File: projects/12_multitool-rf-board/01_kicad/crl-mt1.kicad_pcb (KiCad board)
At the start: 4 copper layers, 68 parts, among them M1 vibro, SW1 RFswitch, SW2 RFswitch, U1 STM32WB55RG, U10 ESD, U5 ST7565R, U9 loadsw, X10 BAT+NTC, X6 FFC 18p, Y1 32MHz, Y2 32.768kHz

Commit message: proj12: transcribe all 8 chip pinouts from datasheets - board complete, 0 pending
Datasheet pads transcribed into pinmap.AUTHORED (with support parts in design.py):
- CC1101 QFN-20 (SWRS061I T19): AVDD x4, GND+EP, +DCOUPL cap
- ST25R3916 UFQFPN-32 (DS12484 Fig4): VDD x8, VSS x6+EP, I2C_EN=GND, AGDC cap,
  SCLK/MISO/MOSI/BSS(SS)/IRQ/RFO1/RFO2/RFI1/RFI2/XTI/XTO mapped exactly
- BQ25896 WQFN-24 (SLUSC76C): +buck inductor, bootstrap, REGN cap, ILIM R, TS divider, CE
- BQ27220 DSBGA-9 (SLUSCB7A): +VDD cap, GPOUT pull-up, BIN pull-down
- LM3281 DSBGA-6 (SNVSA38, was wrongly DSBGA-5): +MODE pin
- LP5562 DSBGA-12 (SNVS820B): +ADDR_SEL0/1, custom 3x4 ball footprint (A1-C4)
- RS3221-3.3 SOT-23-3 (RevA.3, was wrongly DFN-6)

pinmap: multi-pad net support; make_footprints: BGA grid generator.
88 parts, 118 nets, ERC 0 errors; PCB places 87 parts; all pads cross-check clean.

Co-Authored-By: Claude Opus 4.8 <noreply@anthropic.com>
Claude-Session: https://claude.ai/code/session_01Hk6s8R6up8HYVQWXd3atVk
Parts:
- added C_AGDC: 1uF, Capacitor_SMD:C_0402_1005Metric, F.Cu at (47.4, 103.1)
- added C_BTST: 47nF, Capacitor_SMD:C_0402_1005Metric, F.Cu at (70.3, 150.3)
- added C_CCd: 100nF, Capacitor_SMD:C_0402_1005Metric, F.Cu at (44.3, 53.1)
- added C_FGV: 2.2uF, Capacitor_SMD:C_0402_1005Metric, F.Cu at (154.0, 150.3)
- added C_REGN: 4.7uF, Capacitor_SMD:C_0805_2012Metric, F.Cu at (80.5, 150.8)
- added DA7: LP5562, crl-mt1:LP5562_DSBGA12, F.Cu at (163.3, 68.9)
- added DA8: RS3221-3.3, Package_TO_SOT_SMD:SOT-23, F.Cu at (224.6, 151.5)
- added L_CHG: 2.2uH, Inductor_SMD:L_0805_2012Metric, F.Cu at (60.6, 150.7)
- added R_FGB: 10k, Resistor_SMD:R_0402_1005Metric, F.Cu at (172.7, 150.3)
- added R_FGO: 10k, Resistor_SMD:R_0402_1005Metric, F.Cu at (163.3, 150.3)
- added R_ILIM: 1.1k, Resistor_SMD:R_0402_1005Metric, F.Cu at (90.4, 150.3)
- added R_TS1: 5.23k, Resistor_SMD:R_0402_1005Metric, F.Cu at (99.7, 150.3)
- added R_TS2: 30.31k, Resistor_SMD:R_0402_1005Metric, F.Cu at (109.2, 150.3)
- added U2: CC1101, Package_DFN_QFN:QFN-20-1EP_4x4mm_P0.5mm_EP2.5x2.5mm, F.Cu at (34.3, 55.2)
- added U3: ST25R3916, Package_DFN_QFN:QFN-32-1EP_5x5mm_P0.5mm_EP3.1x3.1mm, F.Cu at (35.6, 105.8)
- added U6: BQ25896, Package_DFN_QFN:QFN-24-1EP_4x4mm_P0.5mm_EP2.65x2.65mm, F.Cu at (50.1, 152.5)
- added U7: BQ27220, Package_BGA:BGA-9_1.6x1.6mm_Layout3x3_P0.5mm, F.Cu at (143.6, 151.2)
- added U8: LM3281, Package_BGA:Texas_DSBGA-6_0.76x1.16mm_Layout2x3_P0.4mm, F.Cu at (182.7, 150.7)
- added U8B: LM3281, Package_BGA:Texas_DSBGA-6_0.76x1.16mm_Layout2x3_P0.4mm, F.Cu at (202.8, 150.7)
- moved U9 144.6 mm to (245.7, 151.5)
- moved R37 144.6 mm to (236.3, 151.0)
- moved R_CC2 144.6 mm to (273.5, 150.3)
- moved U10 144.6 mm to (255.0, 151.5)
- moved R_CC1 144.6 mm to (264.0, 150.3)
- moved L14 130.4 mm to (212.8, 150.7)
- moved L13 119.9 mm to (192.7, 150.7)
- moved BT1 69.9 mm to (132.4, 152.0)
- moved X10 69.9 mm to (120.5, 153.0)
- moved ANT_NFC 23.5 mm to (83.2, 104.7)
- moved X_NFC1 23.5 mm to (70.5, 104.1)
- moved ZQ1 23.5 mm to (58.6, 104.2)
- moved FLT2 20.0 mm to (53.0, 53.5)
- moved SW2 20.0 mm to (71.9, 53.9)
- moved J_SUBG 20.0 mm to (99.3, 55.1)
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
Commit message: proj12: board outline + KRT placement inputs (groups/intent)
- make_pcb.py: add 110x46mm rounded board outline (Edge.Cuts)
- make_place_inputs.py: emit crl-mt1.groups.json from functional groups
  (8 groups, 87 parts) for the KiCadRoutingTools placer; check_groups: 0 errors
- crl-mt1.groups.json + crl-mt1.intent.json (floor-plan intent)

First placement pass produced candidates but needs more anneal moves to fully
de-overlap 87 parts; higher-move run in progress.

Co-Authored-By: Claude Opus 4.8 <noreply@anthropic.com>
Claude-Session: https://claude.ai/code/session_01Hk6s8R6up8HYVQWXd3atVk
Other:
- board outline added: 110 x 46 mm

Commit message: proj12: lock connectors/antennas/buttons on board edges for placement
make_pcb.py: 15 edge parts (USB-C, FFC, GPIO header, SWD, battery, U.FL,
3 antennas, 6 buttons) placed on the outline perimeter and KiCad-locked;
unlocked parts piled below the board as the placer's from-scratch start.
This gives the KiCadRoutingTools placer real edge anchors to organize the
functional groups around (the first unanchored run couldn't converge).

Co-Authored-By: Claude Opus 4.8 <noreply@anthropic.com>
Claude-Session: https://claude.ai/code/session_01Hk6s8R6up8HYVQWXd3atVk
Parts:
- moved X10 133.6 mm to (32.0, 53.0), turned to 90 degrees
- moved SW_U 129.0 mm to (110.0, 32.0)
- moved SW_D 127.0 mm to (116.0, 32.0)
- moved SW_L 125.1 mm to (122.0, 32.0)
- moved SW_R 123.3 mm to (128.0, 32.0)
- moved SW_O 109.1 mm to (104.0, 32.0)
- moved SW_B 105.5 mm to (98.0, 32.0)
- moved ANT_LF 99.3 mm to (101.0, 32.0)
- moved J_USB 94.7 mm to (85.0, 74.0)
- moved ANT_NFC 73.1 mm to (91.0, 32.0)
- moved LS1 66.6 mm to (54.1, 172.5)
- moved Q_SPK 66.6 mm to (65.1, 171.7)
- moved Q_VIB 66.6 mm to (43.4, 171.7)
- moved M1 66.6 mm to (34.0, 172.0)
- moved J_GPIO 63.8 mm to (137.5, 53.0), turned to 90 degrees
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
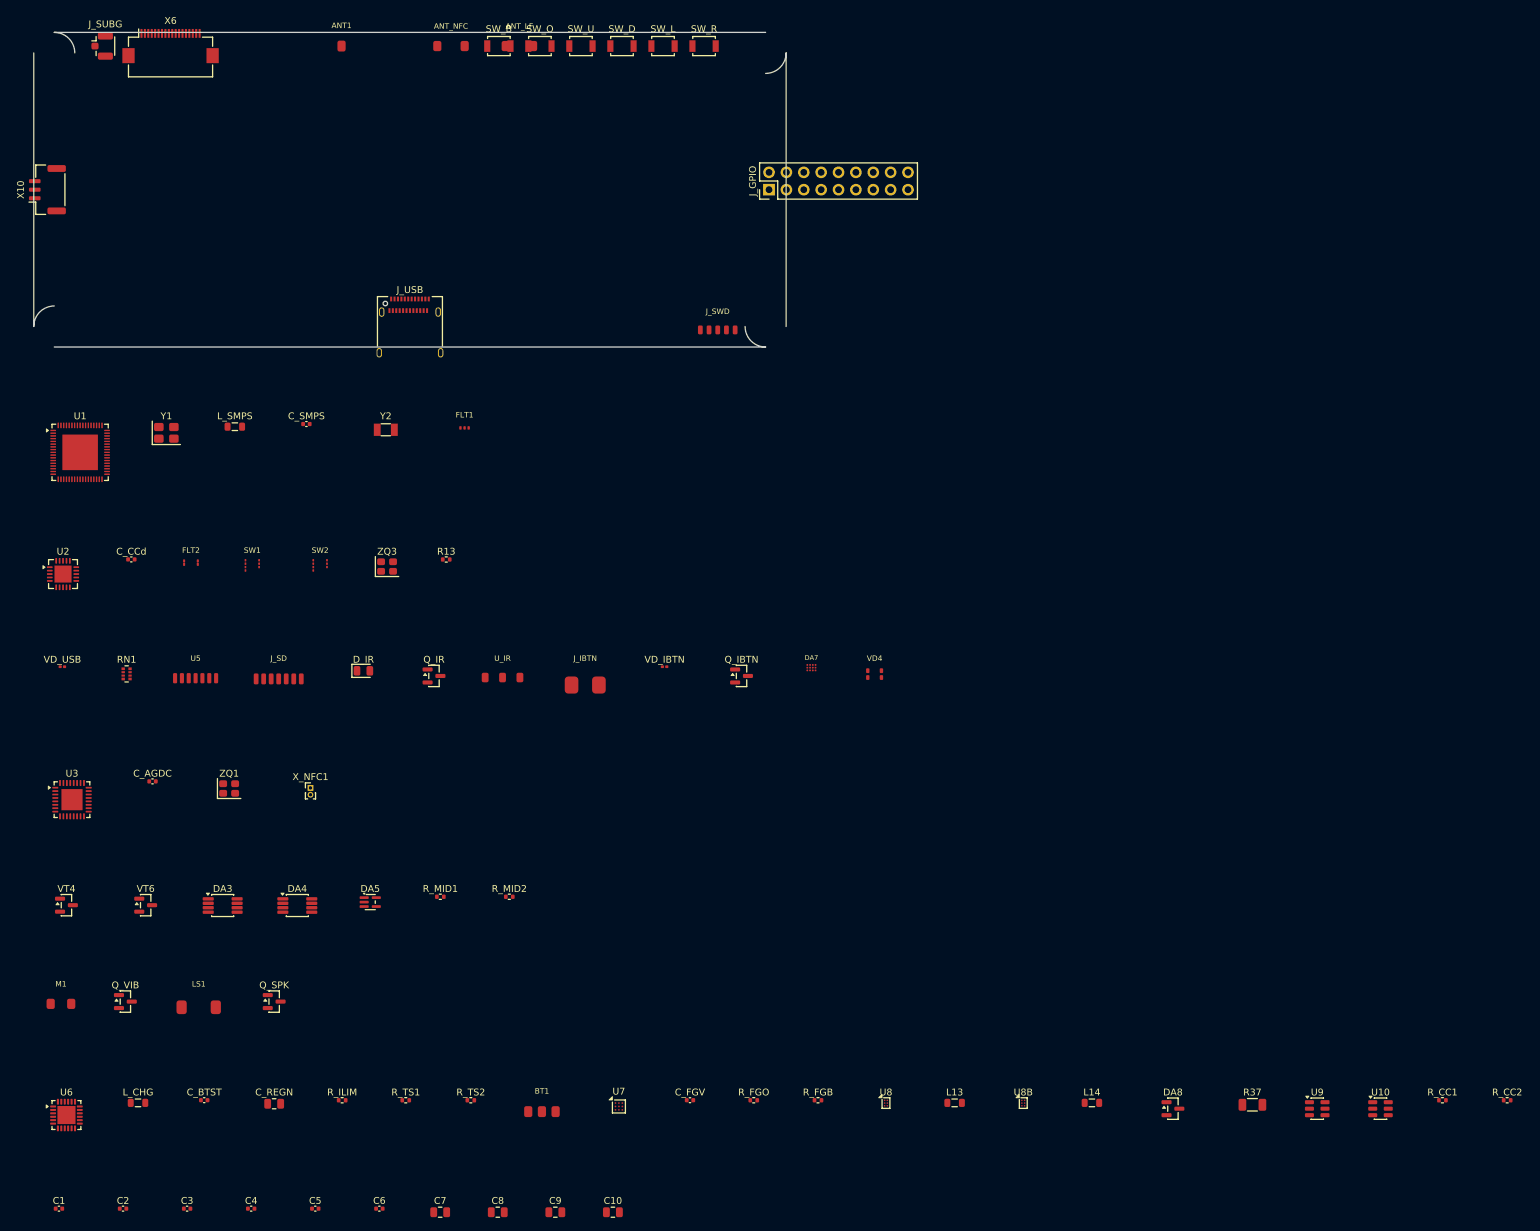
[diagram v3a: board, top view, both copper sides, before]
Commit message: proj12: deterministic legal placement - buildable, 0 overlaps
make_pcb.py: replace stochastic-placer dependence with a deterministic,
legal-by-construction placement - unlocked parts flow in grouped rows inside
an inset interior with courtyard+GAP spacing (no overlaps), connectors locked
on the edges. Closed rectangular outline (arcs left the polygon open ->
containment failed). 150x150mm board sized to hold all 87 parts + routing room.
check_assembly VERDICT: buildable (blocking 0, courtyard 0, 0 off-outline).

The KRT stochastic placer couldn't converge an 87-part board (group-cohesion
weight piled cluster members); the deterministic pack is reliable and feeds
the autorouter directly.

Co-Authored-By: Claude Opus 4.8 <noreply@anthropic.com>
Claude-Session: https://claude.ai/code/session_01Hk6s8R6up8HYVQWXd3atVk
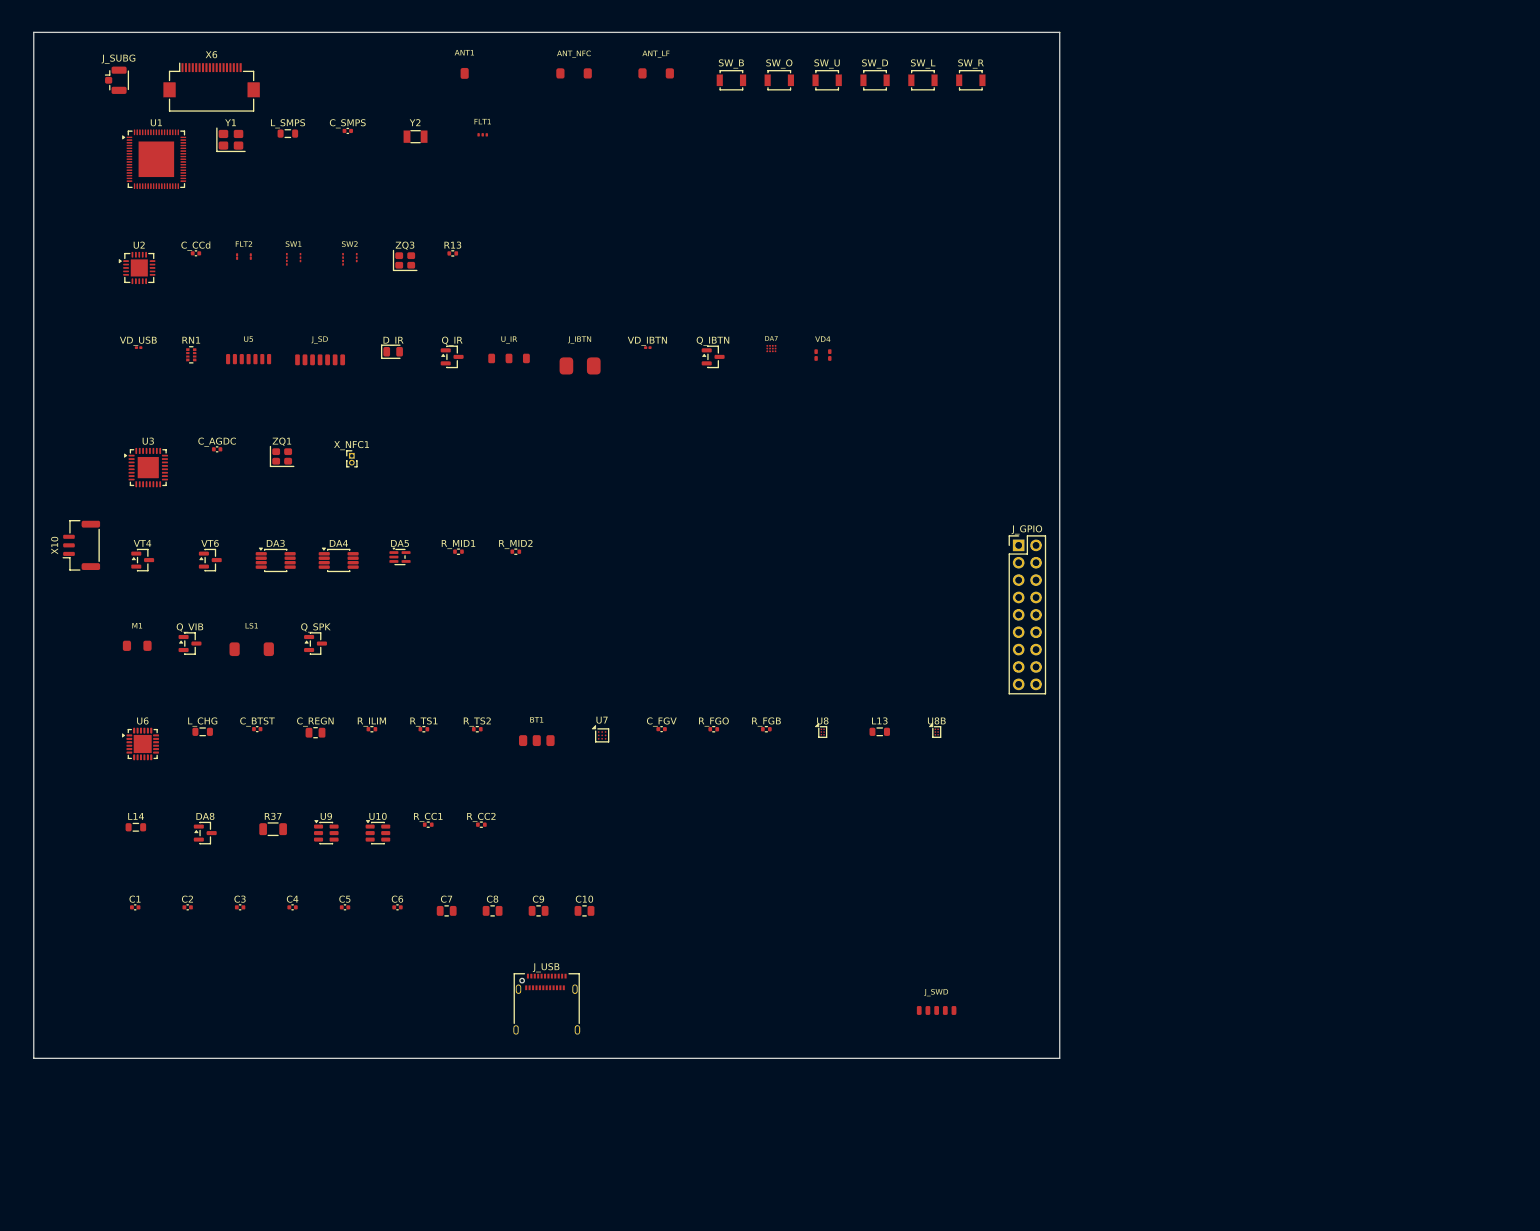
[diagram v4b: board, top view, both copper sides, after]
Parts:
- moved R_CC2 155.3 mm to (95.4, 145.8)
- moved R_CC1 153.7 mm to (87.7, 145.8)
- moved U10 152.0 mm to (80.3, 147.1)
- moved U9 150.4 mm to (72.8, 147.1)
- moved R37 148.7 mm to (65.0, 146.5)
- moved DA8 147.1 mm to (55.1, 147.1)
- moved L14 145.5 mm to (44.9, 146.2)
- moved J_SWD 104.5 mm to (162.0, 173.0)
- moved J_USB 101.0 mm to (105.0, 173.0)
- moved J_GPIO 63.5 mm to (174.0, 105.0), turned to 0 degrees
- moved U8B 55.7 mm to (162.0, 132.3)
- moved U6 55.4 mm to (45.9, 134.0)
- moved L13 55.3 mm to (153.7, 132.3)
- moved L_CHG 55.1 mm to (54.7, 132.3)
- moved U8 55.0 mm to (145.3, 132.3)
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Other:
- board size 110 x 46 mm -> 150 x 150 mm

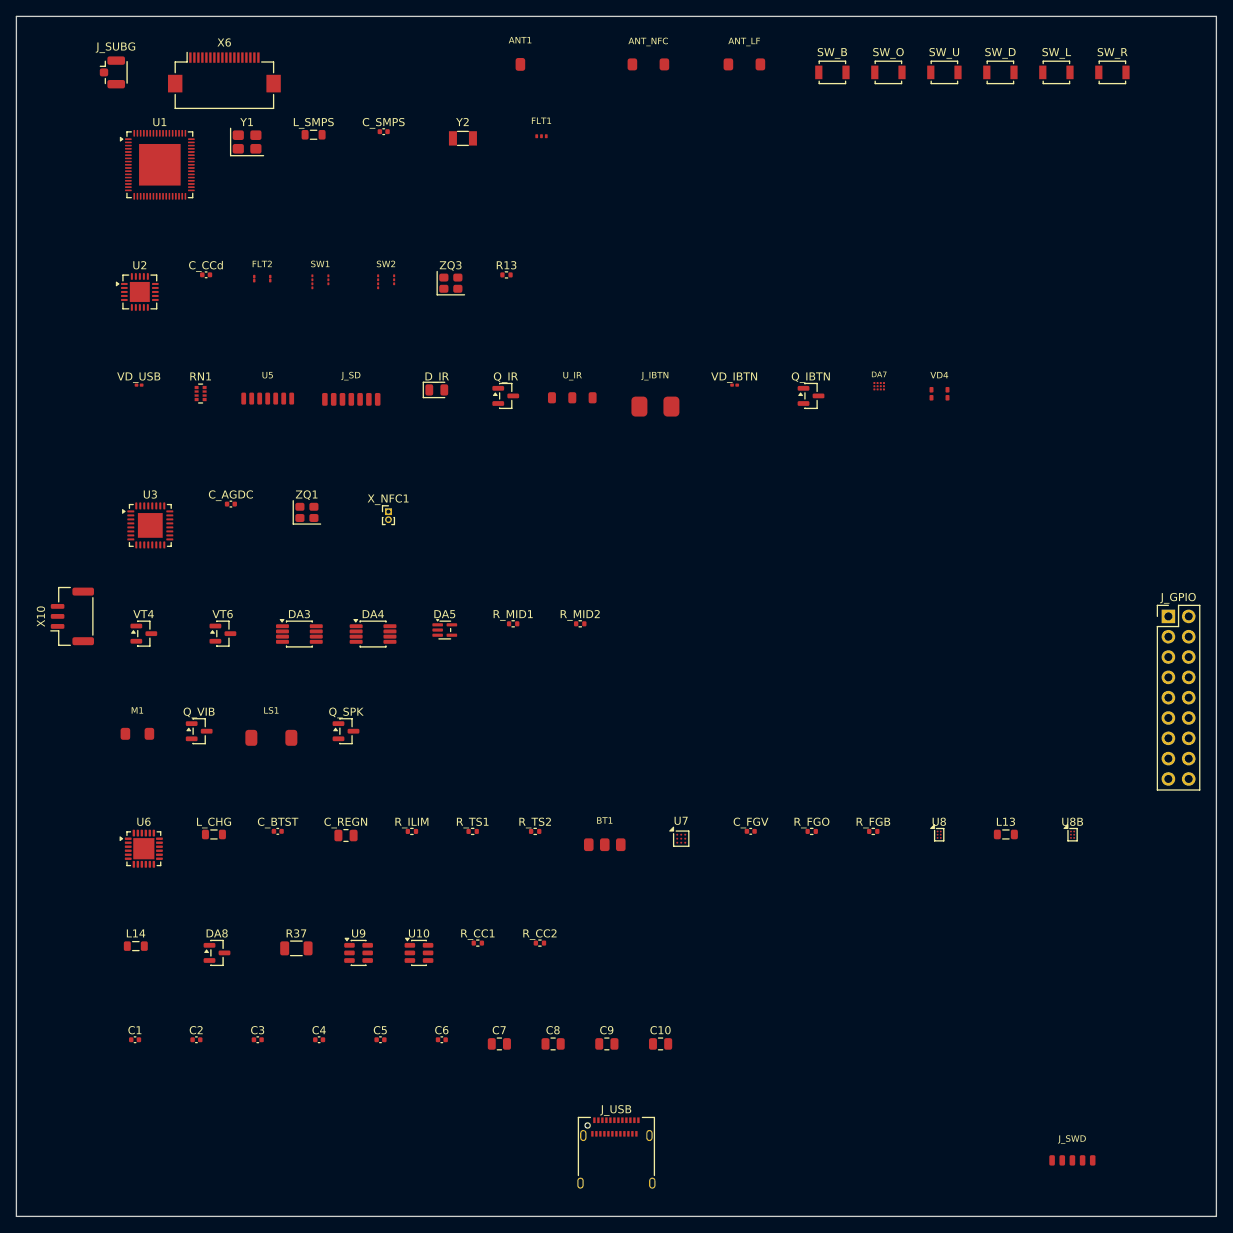
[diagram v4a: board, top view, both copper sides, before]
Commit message: proj12: compact two-sided board (110x66mm) - buildable
Reworked make_pcb.py for a compact, reference-proportion board:
- two-sided assembly: ICs/connectors/crystals on TOP, small passives + SOT-23
  FETs + SC-70 on BOTTOM (flipped), ~halving top-side area
- tighter GAP (1.2mm), largest-first row packing
- top interior inset clear of the left/right edge connectors (X10, J_GPIO);
  edge connectors/antennas/buttons respaced for the 110mm width
- board 110x66mm (was 150x150) ~ 1/3 the area; still original (own outline,
  no mascot/trademark)
check_assembly VERDICT: buildable (0 overlap, 0 pad-conflict, 0 off-board).
Routing the compact board in progress.

Co-Authored-By: Claude Opus 4.8 <noreply@anthropic.com>
Claude-Session: https://claude.ai/code/session_01Hk6s8R6up8HYVQWXd3atVk
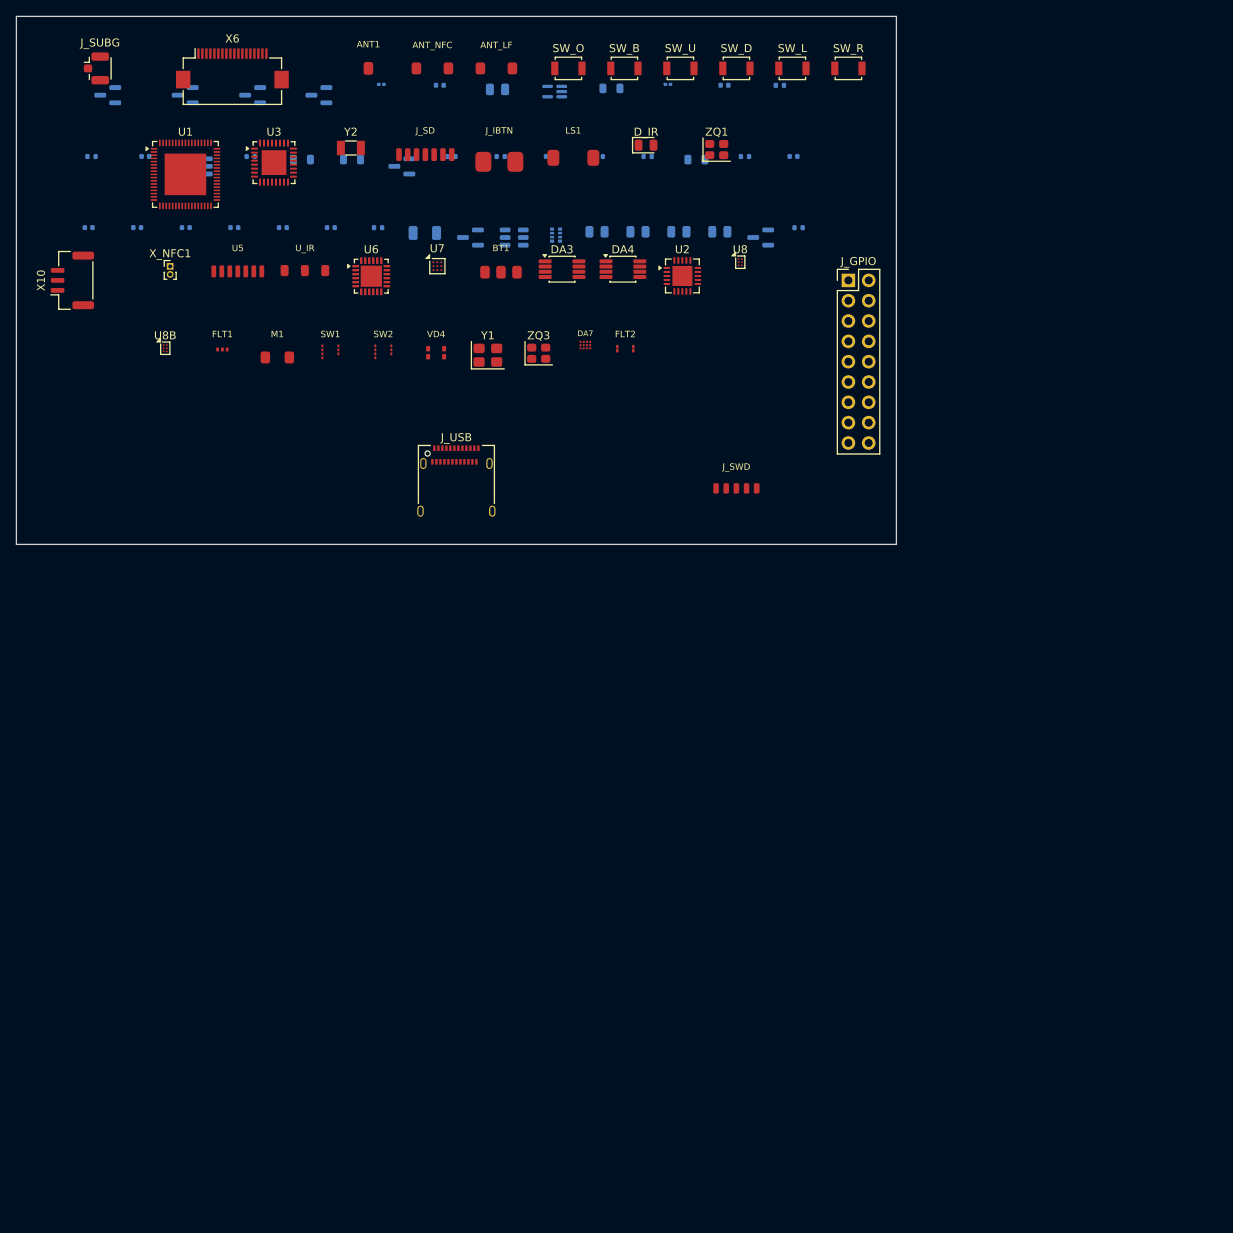
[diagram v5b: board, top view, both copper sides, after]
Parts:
- C1, C10, C2, C3, C4, C5, C6, C7, C8, C9, C_AGDC, C_BTST, C_CCd, C_FGV, C_REGN, C_SMPS, DA5, DA8, L13, L14, L_CHG, L_SMPS, Q_IBTN, Q_IR, Q_SPK, Q_VIB, R13, R37, RN1, R_CC1, R_CC2, R_FGB, R_FGO, R_ILIM, R_MID1, R_MID2, R_TS1, R_TS2, U10, U9, VD_IBTN, VD_USB, VT4, VT6: moved to B.Cu
- moved C1 137.7 mm to (127.1, 47.5), turned to 180 degrees
- moved U8B 128.7 mm to (48.6, 71.5)
- moved L13 121.9 mm to (65.7, 47.9), turned to 180 degrees
- moved DA8 108.1 mm to (41.4, 39.8), turned to 180 degrees
- moved L_CHG 103.7 mm to (115.0, 47.9), turned to 180 degrees
- moved C6 103.4 mm to (63.3, 56.4), turned to 180 degrees
- moved C5 103.2 mm to (57.2, 56.4), turned to 180 degrees
- moved C4 102.9 mm to (51.2, 56.4), turned to 180 degrees
- moved C3 102.6 mm to (45.1, 56.4), turned to 180 degrees
- moved C2 102.4 mm to (39.0, 56.4), turned to 180 degrees
- moved C7 102.3 mm to (102.6, 56.9), turned to 180 degrees
- moved C8 102.1 mm to (107.7, 56.9), turned to 180 degrees
- moved L14 102.0 mm to (72.0, 47.9), turned to 180 degrees
- moved C9 101.9 mm to (112.8, 56.9), turned to 180 degrees
- moved C10 101.8 mm to (117.9, 56.9), turned to 180 degrees
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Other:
- board size 150 x 150 mm -> 110 x 66 mm
